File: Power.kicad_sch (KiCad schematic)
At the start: 77 parts, among them P3 CONN_1, P4 CONN_1, P5 CONN_1, P6 CONN_1, P7 CONN_1, P8 CONN_10X2, P9 POWER_SW, SW1 POWER, U1 74LS04, U10 74HCT14, U11 74LS06, U12 74LS00, U13 74LS74, U4 74LS86, U5 74LS02, U6 74LS00, U7 74LS32

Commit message: Schematic in progress
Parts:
- removed U11: 74LS06, DIP-14__300, symbol 74xx:74LS06
- added U10, U11, U12, U16: 74LS32, Package_DIP:DIP-14_W7.62mm_Socket_LongPads, symbol 74xx:74LS32
- added U13, U14: 74LS07, Package_DIP:DIP-14_W7.62mm_Socket_LongPads, symbol 74xx:74LS07
- added U15: 74LS08, Package_DIP:DIP-14_W7.62mm_Socket_LongPads, symbol 74xx:74LS08
- added U17: 74LS14, Package_DIP:DIP-14_W7.62mm_Socket_LongPads, symbol 74xx:74LS14
- added U18: 74LS06, Package_DIP:DIP-14_W7.62mm_Socket_LongPads, symbol 74xx:74LS06
- added U20: 74LS04, Package_DIP:DIP-14_W7.62mm_Socket_LongPads, symbol 74xx:74LS04
- C1, C2, C28, C3, C35, C4: footprint C1V5 -> Capacitor_THT:CP_Radial_D5.0mm_P2.50mm
- C10, C11, C12, C13, C14, C15, C16, C17, C18, C19, C20, C21, C22, C23, C24, C25, C26, C27, C29, C30, C31, C32, C33, C34, C36, C37, C38, C39, C40, C41, C42, C43, C44, C45, C46, C47, C48, C49, C5, C50, C51, C52, C53, C54, C55, C6, C7, C8, C9: footprint C2 -> Capacitor_THT:C_Disc_D5.0mm_W2.5mm_P5.00mm
- D1, D2: footprint D3 -> Diode_THT:D_DO-41_SOD81_P10.16mm_Horizontal
- P2: renamed from P3; footprint 1pin -> MountingHole:MountingHole_2.7mm_M2.5_Pad_TopBottom
- P3: renamed from P4; footprint 1pin -> MountingHole:MountingHole_2.7mm_M2.5_Pad_TopBottom
- P4: renamed from P5; footprint 1pin -> MountingHole:MountingHole_2.7mm_M2.5_Pad_TopBottom
- P5: renamed from P6; footprint 1pin -> MountingHole:MountingHole_2.7mm_M2.5_Pad_TopBottom
- P6: renamed from P7; footprint 1pin -> MountingHole:MountingHole_2.7mm_M2.5_Pad_TopBottom
- P7: renamed from P8; footprint ATX_NON_90DEG -> Custom:ATXConnector
- P8: renamed from P9; footprint PIN_ARRAY_2X1 -> Connector_PinHeader_2.54mm:PinHeader_1x02_P2.54mm_Vertical
- R1: renamed from R2; footprint R3 -> Resistor_THT:R_Axial_DIN0207_L6.3mm_D2.5mm_P7.62mm_Horizontal
- R2: renamed from R3; footprint R3 -> Resistor_THT:R_Axial_DIN0207_L6.3mm_D2.5mm_P7.62mm_Horizontal
- R3: renamed from R4; footprint R3 -> Resistor_THT:R_Axial_DIN0207_L6.3mm_D2.5mm_P7.62mm_Horizontal
- SW1: footprint SW_PUSH_SMALL -> Button_Switch_THT:SW_Tactile_Straight_KSL0Axx1LFTR
- U1, U4, U5, U6, U7: footprint DIP-14__300 -> Package_DIP:DIP-14_W7.62mm_Socket_LongPads
- U19: renamed from U10; footprint DIP-14__300 -> Package_DIP:DIP-14_W7.62mm_Socket_LongPads
- U21: renamed from U12; footprint DIP-14__300 -> Package_DIP:DIP-14_W7.62mm_Socket_LongPads
- U22: renamed from U13; footprint (none) -> Package_DIP:DIP-14_W7.62mm_Socket_LongPads
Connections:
- net GND: now also U10.7 (GND), U11.7 (GND), U12.7 (GND), U13.7 (GND), U14.7 (GND), U15.7 (GND), U16.7 (GND), U17.7 (GND), U18.7 (GND), U20.7 (GND)
- net VCC: now also U10.14 (VCC), U11.14 (VCC), U12.14 (VCC), U13.14 (VCC), U14.14 (VCC), U15.14 (VCC), U16.14 (VCC), U17.14 (VCC), U18.14 (VCC), U20.14 (VCC)
- net -5V: now reaches P7.16 (Pin_16)
- net +12V: now reaches P7.19 (Pin_19)
- net -12V: now reaches P7.4 (Pin_4)
- no-connect marks 6 -> 3
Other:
- company: N8VEM Users Group -> (none)
- title: 6809 and 6502 ATX and 6U -> 6809PC

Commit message: PCB in progress
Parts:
- added P10, P21, P22, P23, P4, P8, P9: CONN_1, MountingHole:MountingHole_3.2mm_M3_Pad_TopBottom, symbol Mechanical:MountingHole_Pad
- C1, C2, C28, C3, C35, C4: footprint Capacitor_THT:CP_Radial_D5.0mm_P2.50mm -> Custom:STD_DDW_PCAP
- C10, C11, C12, C13, C14, C15, C16, C17, C18, C19, C20, C21, C22, C23, C24, C25, C26, C27, C29, C30, C31, C32, C33, C34, C36, C37, C38, C39, C40, C41, C42, C43, C44, C45, C46, C47, C48, C49, C5, C50, C51, C52, C53, C54, C55, C6, C7, C8, C9: footprint Capacitor_THT:C_Disc_D5.0mm_W2.5mm_P5.00mm -> Custom:STD_DDW_CAP
- D1, D2: footprint Diode_THT:D_DO-41_SOD81_P10.16mm_Horizontal -> Custom:STD_DDW_DIODE
- P12: renamed from P8; footprint Connector_PinHeader_2.54mm:PinHeader_1x02_P2.54mm_Vertical -> Custom:STD_DDW_PINHEAD_V_1x02
- P2, P3: footprint MountingHole:MountingHole_2.7mm_M2.5_Pad_TopBottom -> MountingHole:MountingHole_3.2mm_M3_Pad_TopBottom
- P5: renamed from P4; footprint MountingHole:MountingHole_2.7mm_M2.5_Pad_TopBottom -> MountingHole:MountingHole_3.2mm_M3_Pad_TopBottom
- P6: renamed from P5; footprint MountingHole:MountingHole_2.7mm_M2.5_Pad_TopBottom -> MountingHole:MountingHole_3.2mm_M3_Pad_TopBottom
- P7: renamed from P6; footprint MountingHole:MountingHole_2.7mm_M2.5_Pad_TopBottom -> MountingHole:MountingHole_3.2mm_M3_Pad_TopBottom
- R1, R2, R3: footprint Resistor_THT:R_Axial_DIN0207_L6.3mm_D2.5mm_P7.62mm_Horizontal -> Custom:STD_DDW_RESISTOR
- SW1: footprint Button_Switch_THT:SW_Tactile_Straight_KSL0Axx1LFTR -> Custom:STD_DDW_TACTSW
- U1, U10, U11, U12, U13, U14, U15, U16, U17, U18, U19, U20, U21, U22, U4, U5, U6, U7: footprint Package_DIP:DIP-14_W7.62mm_Socket_LongPads -> Custom:STD_DDW_DIP14
- renumbered P7 to P11
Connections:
- net GND: now also P10.1, P21.1, P22.1, P23.1, P4.1, P8.1, P9.1

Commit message: V1.1
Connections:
- net VCC renamed +5V
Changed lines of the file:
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@@
 	)
 	(junction
+		(at 151.13 72.39)
+		(diameter 0)
+		(color 0 0 0 0)
+	)
+	(junction
 		(at 238.76 222.25)
 		(diameter 0)
@@
 	(wire
 		(pts
-			(xy 114.3 72.39) (xy 152.4 72.39)
+			(xy 114.3 72.39) (xy 151.13 72.39)
 		)
 		(stroke
@@
 	(wire
 		(pts
+			(xy 151.13 72.39) (xy 152.4 72.39)
+		)
+		(stroke
+			(width 0)
+			(type default)
+		)
+	)
+	(wire
+		(pts
 			(xy 161.29 176.53) (xy 173.99 176.53)
 		)
@@
 				)
 			)
+		)
+	)
+	(symbol
+		(lib_id "power:+5V")
+		(at 151.13 72.39 0)
+		(unit 1)
+		(exclude_from_sim no)
+		(in_bom yes)
+		(on_board yes)
+		(dnp no)
+		(fields_autoplaced yes)
+		(property "Reference" "#PWR0210"
+			(at 151.13 76.2 0)
+			(effects
+				(font
+					(size 1.27 1.27)
+				)
+				(hide yes)
+			)
+		)
+		(property "Value" "+5V"
+			(at 151.13 67.31 0)
+			(effects
+				(font
+					(size 1.27 1.27)
+				)
+			)
+		)
+		(property "Footprint" ""
+			(at 151.13 72.39 0)
+			(effects
+				(font
+					(size 1.27 1.27)
+				)
+				(hide yes)
+			)
+		)
+		(property "Datasheet" ""
+			(at 151.13 72.39 0)
+			(effects
+				(font
+					(size 1.27 1.27)
+				)
+				(hide yes)
+			)
+		)
+		(property "Description" "Power symbol creates a global label with name \"+5V\""
+			(at 151.13 72.39 0)
+			(effects
+				(font
+					(size 1.27 1.27)
+				)
+				(hide yes)
+			)
+		)
+		(pin "1"
+		)
+		(instances
+			(project ""
+				(path "/d94f9d60-5ece-4752-b49c-b0d1c95f35bc/00000000-0000-0000-0000-0000526d2858"
+					(reference "#PWR0210")
+					(unit 1)
+				)
+			)

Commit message: 6809PC work
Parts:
- removed C17, C34, C55: 0.1 uF, Custom:STD_DDW_CAP, symbol Device:C
- removed U11, U12: 74LS32, Custom:STD_DDW_DIP14, symbol 74xx:74LS32
- removed U13, U14: 74LS07, Custom:STD_DDW_DIP14, symbol 74xx:74LS07
- removed U20: 74LS04, Custom:STD_DDW_DIP14, symbol 74xx:74LS04
- added C17: 22 uF, Custom:STD_DDW_PCAP, symbol Device:C_Polarized
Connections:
- net +5V: now also C17.1
- net GND: now also C17.2

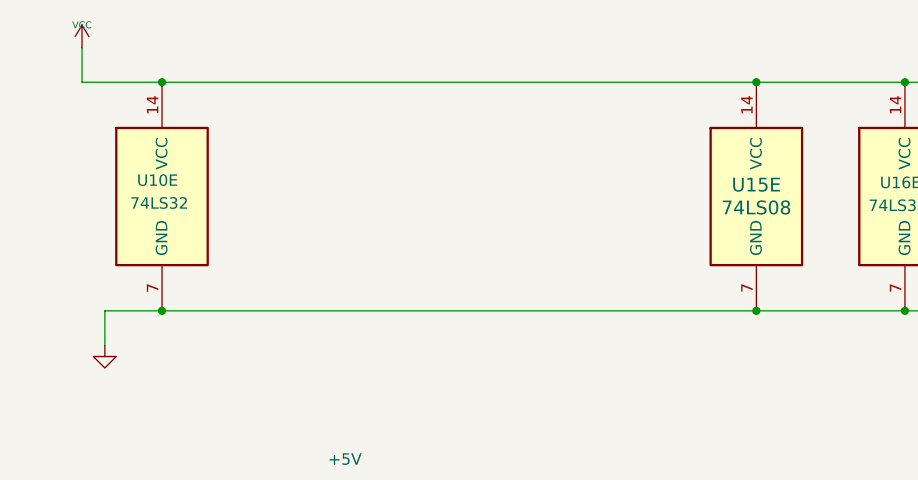
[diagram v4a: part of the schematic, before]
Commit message: fix bus issue
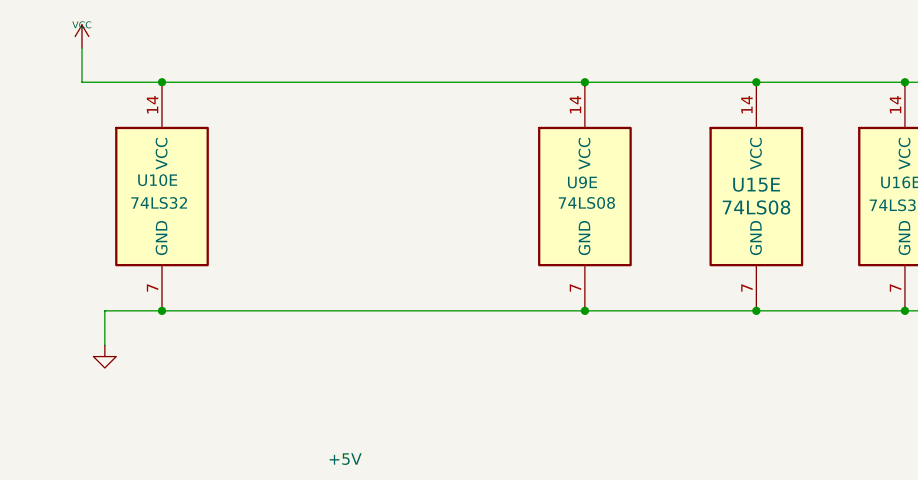
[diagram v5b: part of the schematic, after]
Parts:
- added U9: 74LS08, Custom:STD_DDW_DIP14, symbol 74xx:74LS08
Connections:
- net +5V: now also U9.14 (VCC)
- net GND: now also U9.7 (GND)
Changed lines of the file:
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@@
 	(title_block
 		(title "6809PC")
-		(date "2025-05-17")
-		(rev "002")
+		(date "2025-05-31")
+		(rev "003")
 		(comment 1 "https://github.com/danwerner21/6809PC")
 		(comment 2 "Based on work by Andrew Lynch and John Coffman")
@@
 	)
 	(junction
+		(at 177.8 50.8)
+		(diameter 0)
+		(color 0 0 0 0)
+	)
+	(junction
 		(at 238.76 207.01)
 		(diameter 0)
@@
 	)
 	(junction
+		(at 177.8 25.4)
+		(diameter 0)
+		(color 0 0 0 0)
+	)
+	(junction
 		(at 161.29 222.25)
 		(diameter 0)
@@
 	(wire
 		(pts
+			(xy 177.8 50.8) (xy 196.85 50.8)
+		)
+		(stroke
+			(width 0)
+			(type default)
+		)
+	)
+	(wire
+		(pts
 			(xy 114.3 102.87) (xy 123.19 102.87)
 		)
@@
 	(wire
 		(pts
-			(xy 130.81 50.8) (xy 196.85 50.8)
+			(xy 130.81 50.8) (xy 177.8 50.8)
 		)
 		(stroke
@@
 	(wire
 		(pts
-			(xy 130.81 25.4) (xy 196.85 25.4)
+			(xy 130.81 25.4) (xy 177.8 25.4)
 		)
 		(stroke
@@
 		)
 	)
+	(wire
+		(pts
+			(xy 177.8 25.4) (xy 196.85 25.4)
+		)
+		(stroke
+			(width 0)
+			(type default)
+		)
+	)
 	(polyline
 		(pts
@@
 				)
 			)
+		)
+	)
+	(symbol
+		(lib_id "74xx:74LS08")
+		(at 177.8 38.1 0)
+		(unit 5)
+		(exclude_from_sim no)
+		(in_bom yes)
+		(on_board yes)
+		(dnp no)
+		(property "Reference" "U9"
+			(at 175.768 36.576 0)
+			(effects
+				(font
+					(size 1.27 1.27)
+				)
+				(justify left)
+			)
+		)
+		(property "Value" "74LS08"
+			(at 174.752 38.862 0)
+			(effects
+				(font
+					(size 1.27 1.27)
+				)
+				(justify left)
+			)
+		)
+		(property "Footprint" "Custom:STD_DDW_DIP14"
+			(at 177.8 38.1 0)
+			(effects
+				(font
+					(size 1.27 1.27)
+				)
+				(hide yes)
+			)
+		)
+		(property "Datasheet" "http://www.ti.com/lit/gpn/sn74LS08"
+			(at 177.8 38.1 0)
+			(effects
+				(font
+					(size 1.27 1.27)
+				)
+				(hide yes)
+			)
+		)
+		(property "Description" "Quad And2"
+			(at 177.8 38.1 0)
+			(effects
+				(font
+					(size 1.27 1.27)
+				)
+				(hide yes)
+			)
+		)
+		(pin "4"
+		)
+		(pin "8"
+		)
+		(pin "13"
+		)
+		(pin "14"
+		)
+		(pin "2"
+		)
+		(pin "11"
+		)
+		(pin "1"
+		)
+		(pin "10"
+		)
+		(pin "6"
+		)
+		(pin "9"
+		)
+		(pin "7"
+		)
+		(pin "12"
+		)
+		(pin "3"
+		)
+		(pin "5"
+		)
+		(instances
+			(project "6809PC-6U"
+				(path "/d94f9d60-5ece-4752-b49c-b0d1c95f35bc/00000000-0000-0000-0000-0000526d2858"
+					(reference "U9")
+					(unit 5)
+				)
+			)

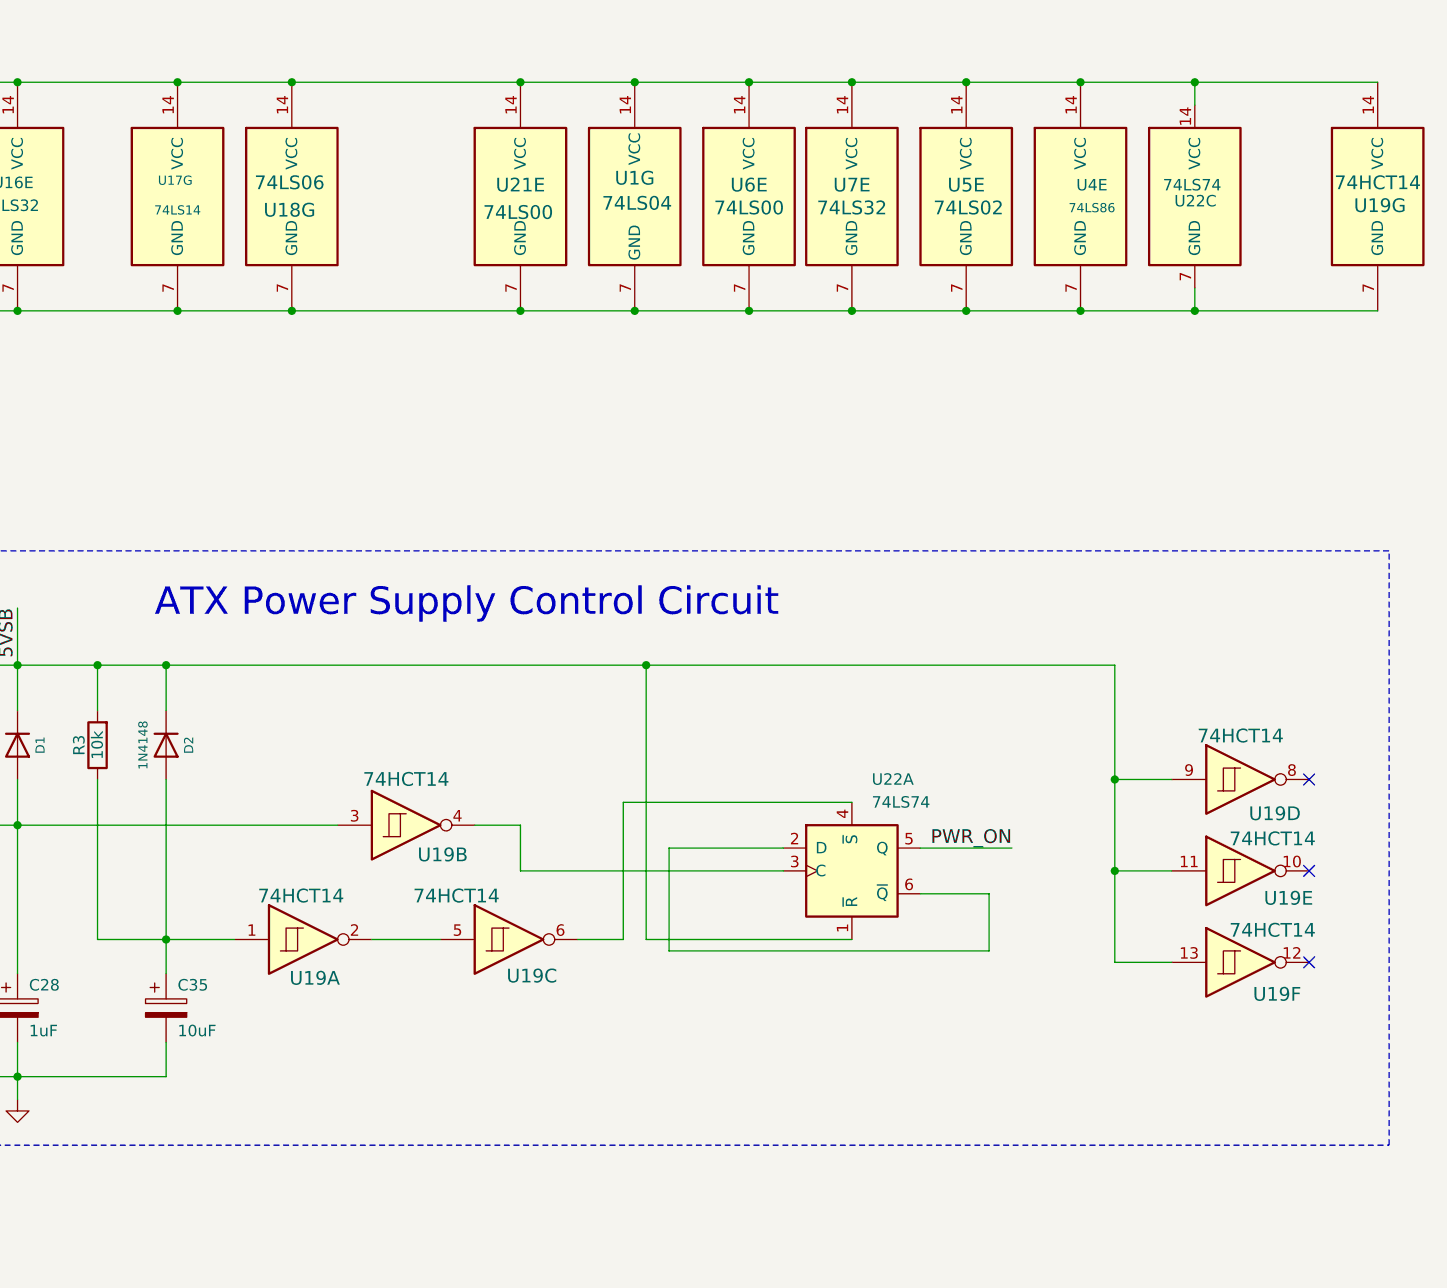
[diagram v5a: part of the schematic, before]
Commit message: fix power supply switch circuit
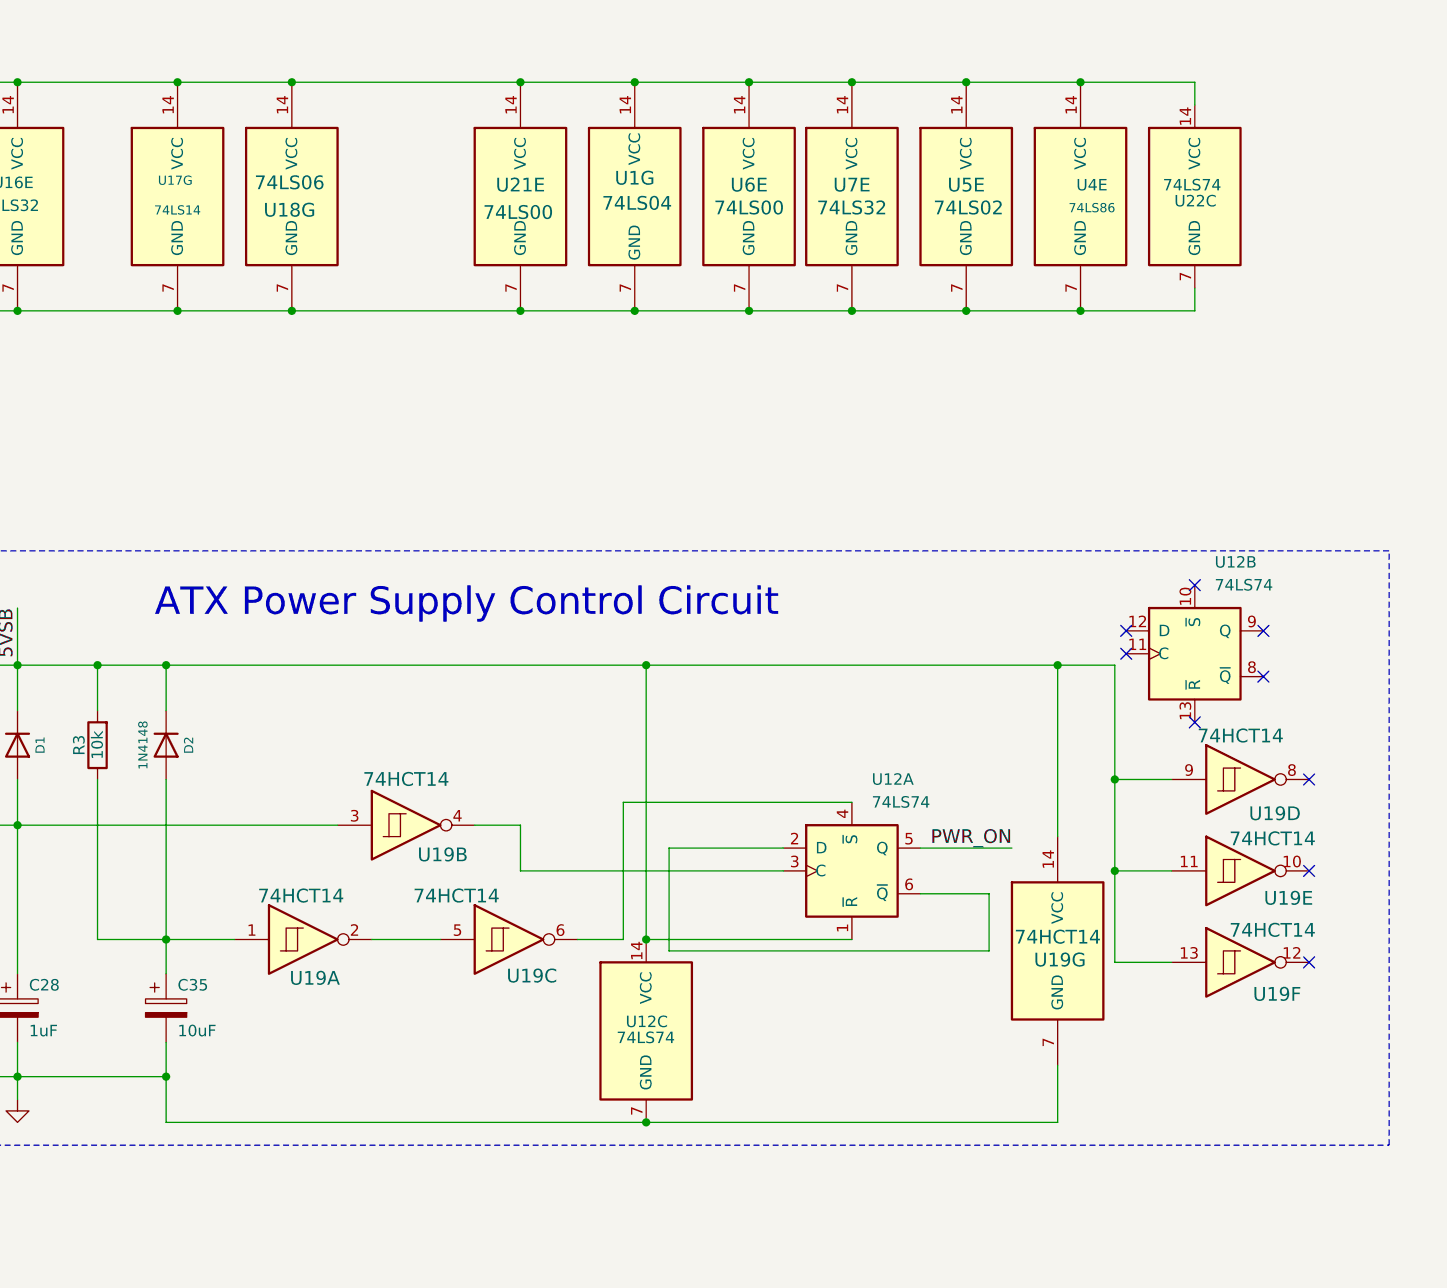
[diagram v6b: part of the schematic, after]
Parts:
- removed unit 1 of U22
- added U12: 74LS74, Custom:STD_DDW_DIP14, symbol 74xx:74LS74
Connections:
- net +5V: no longer U19.14 (VCC)
- net 5VSB: now also U19.14 (VCC), U12.1 (~{R}), U12.14 (VCC)
- net GND: now also U12.7 (GND)
- net PWR_ON: now also U12.5 (Q)
- net at U19.6: now also U12.4 (~{S})
- net at U19.4: now also U12.3 (C)
- new net: U12.2 (D), U12.6 (~{Q})
- no-connect marks 3 -> 9
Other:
- moved on the sheet: U19G
